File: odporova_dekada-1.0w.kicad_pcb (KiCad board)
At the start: 2 copper layers, 196.8 x 195.6 mm, 135 parts, among them J1 Conn_01x01, J2 Conn_01x01, U1 , U10 , U11 , U12 , U13 , U14 , U15 , U16 , U17 , U18 , U19 , U2 , U20 , U21 , U22 , U23 , U24 , U25 , U26 , U27 , U28 , U29 , U3 , U30 , U31 , U32 , U33 , U34 , U35 , U36 , U37 , U38 , U39 , U4 , U40 , U41 , U42 , U43 , U44 , U45 , U46 , U47 , U48 , U49 , U5 , U50 , U51 , U52 , U53 , U54 , U55 , U56 , U57 , U58 , U59 , U6 , U60 , U61 , U62 , U63 , U64 , U65 , U66 , U67 , U68 , U69 , U7 , U70 , U8 , U9 

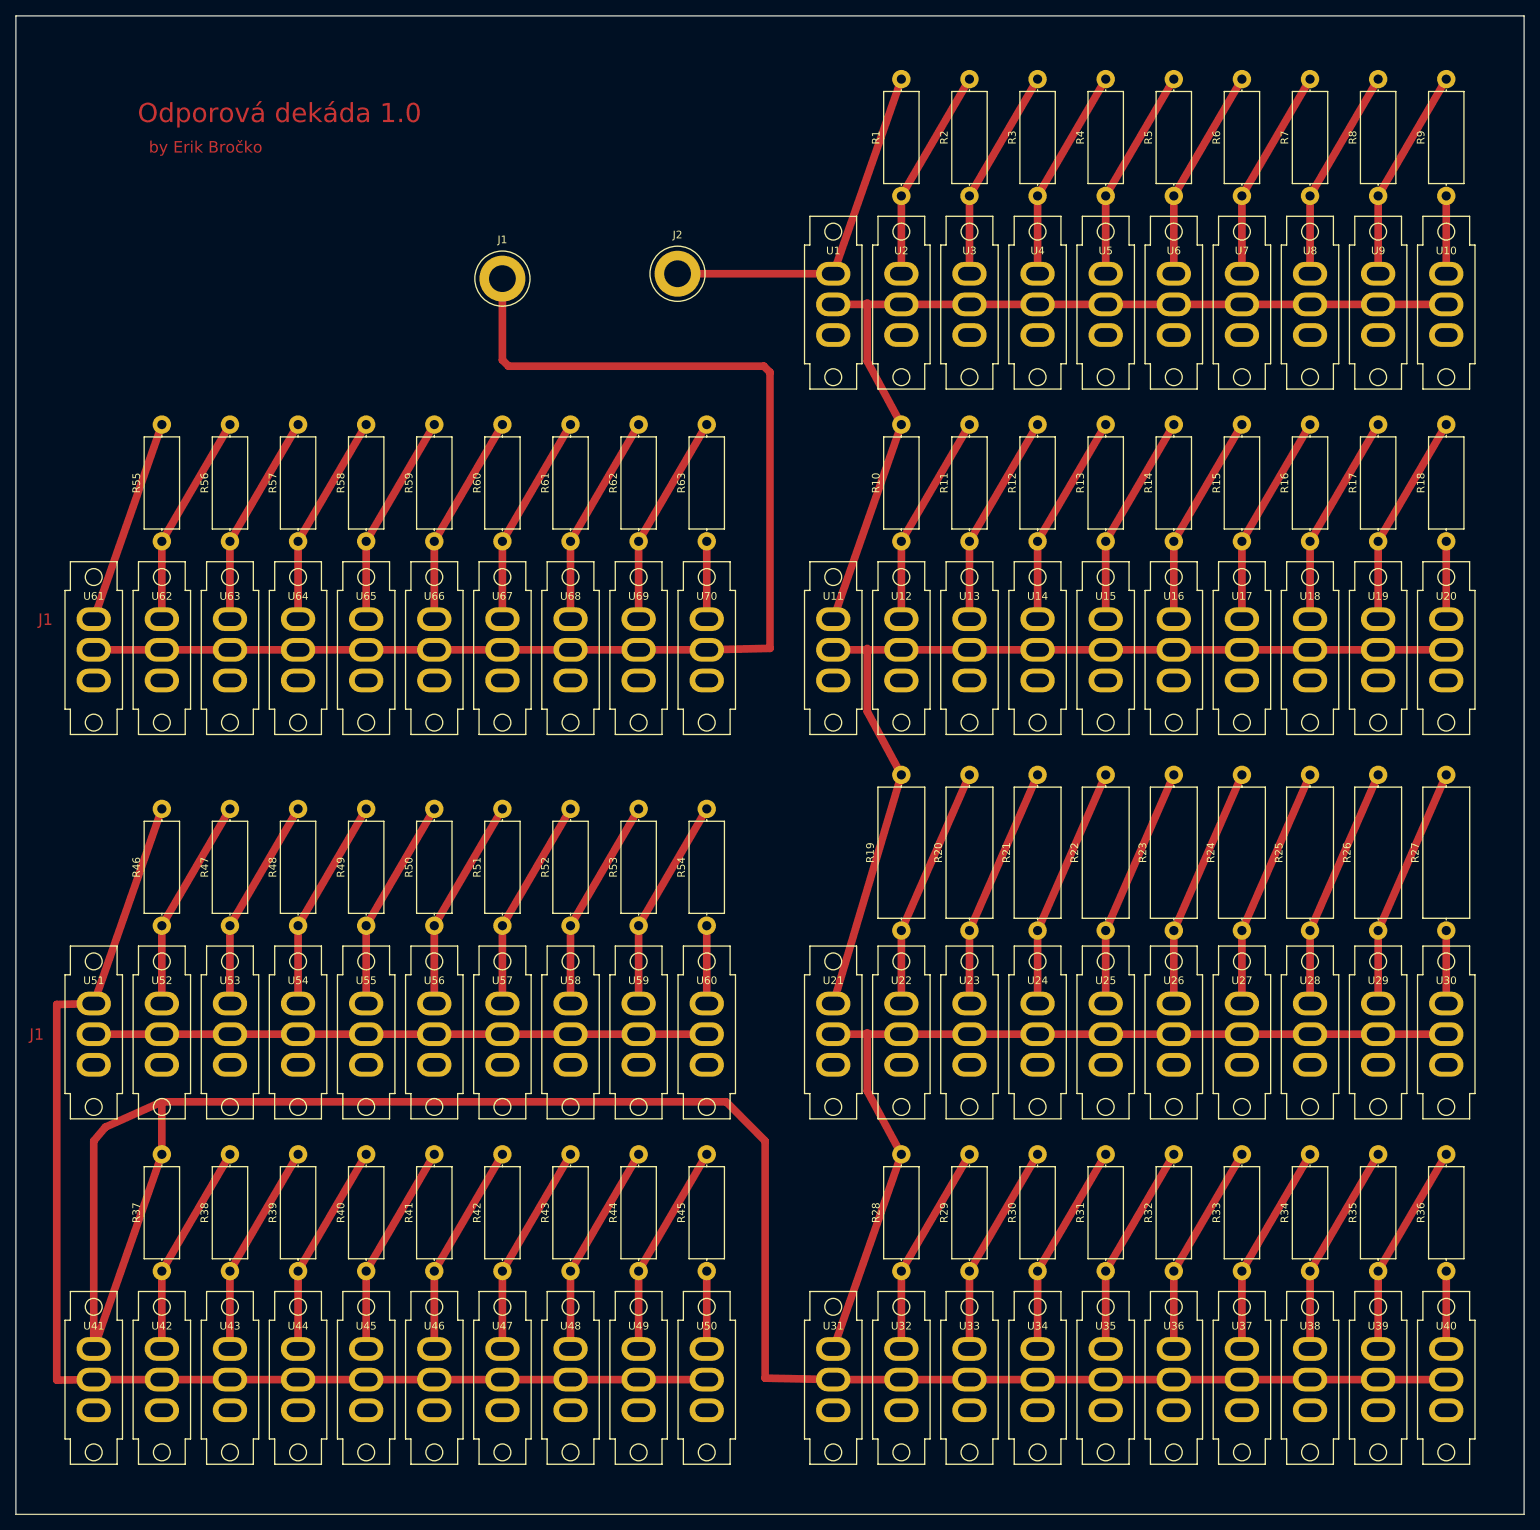
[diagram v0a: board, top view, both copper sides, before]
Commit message: Widened tracks
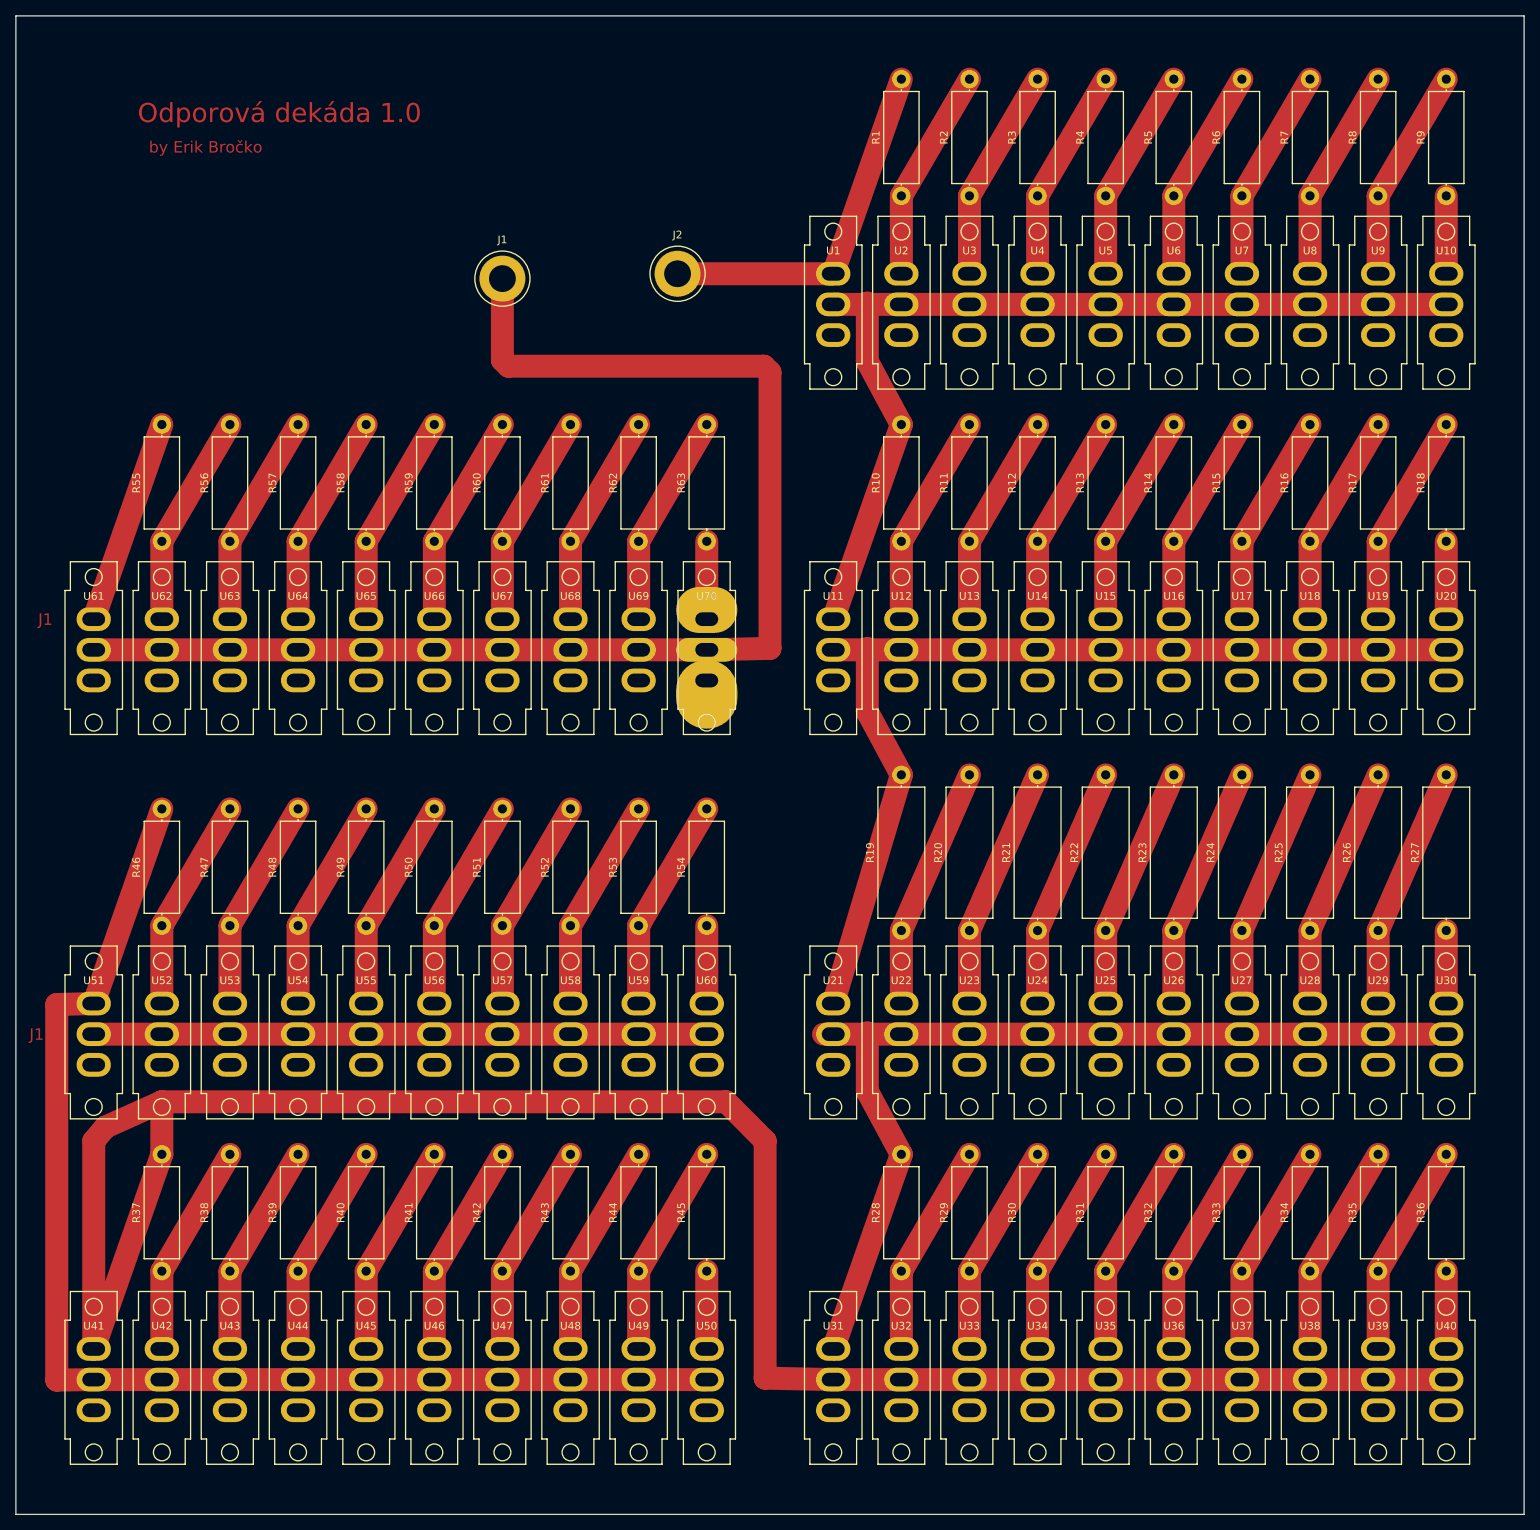
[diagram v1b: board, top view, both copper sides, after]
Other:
- net class Default: trace_width 1 -> 3
